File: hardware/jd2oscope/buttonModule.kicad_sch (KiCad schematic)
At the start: 1 part

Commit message: feat: lot of progress
added decoupling caps, implemented a lot more of the comm. protocol stuffs, updated BNC connector to updated version, added more notes for GPIO pin I/O for future code implementation, lot of other stuff too (frankly can't remember all of it lol); I commit here b/c want to back up progress b/4 I go get smth to eat ;)
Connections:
- net GND: now reaches S1.1
- net GPIOpin: now reaches S1.3
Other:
- note added: "How the button works w/ any given GPIO pin: (GPIO pin's initial state should be set as "HIGH" in the code) an interrupt should be set to trigger if GPIO drops below a certain V (i.e., 0V to represent GND; thus: whenever the button is pressed down, the interrupt is triggered & allows us to execute code from it"
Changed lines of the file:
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@@
 	(generator_version "8.0")
 	(paper "A4")
+	(rectangle
+		(start 119.38 75.692)
+		(end 189.865 86.487)
+		(stroke
+			(width 0)
+			(type default)
+		)
+		(fill
+			(type none)
+		)
+	)
+	(text "How the button works w/ any given GPIO pin:\n(GPIO pin's initial state should be set as \"HIGH\" in the code)\nan interrupt should be set to trigger if GPIO drops below a certain V\n(i.e., 0V to represent GND; thus: whenever the button is pressed down,\nthe interrupt is triggered & allows us to execute code from it"
+		(exclude_from_sim no)
+		(at 120.015 81.28 0)
+		(effects
+			(font
+				(size 1.27 1.27)
+			)
+			(justify left)
+		)
+	)
+	(hierarchical_label "GPIOpin"
+		(shape passive)
+		(at 144.78 97.79 180)
+		(effects
+			(font
+				(size 1.27 1.27)
+			)
+			(justify right)
+		)
+	)
+	(hierarchical_label "GND"
+		(shape passive)
+		(at 160.02 97.79 0)
+		(effects
+			(font
+				(size 1.27 1.27)
+			)
+			(justify left)
+		)
+	)
 	(symbol
 		(lib_id "bttn:KMR731NGLFS")

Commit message: feat: finished schematics
I think! Subject to change tho! for now though at least, I think they look clean asf hah~
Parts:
- renumbered S1 to S4
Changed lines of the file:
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@@
 		(dnp no)
 		(fields_autoplaced yes)
-		(property "Reference" "S1"
+		(property "Reference" "S4"
 			(at 152.4 90.17 0)
 			(effects
@@
 		)
 		(instances
-			(project ""
-				(path "/eb18a3da-9fbf-4329-a814-1afab785c817/53a41818-3f0f-42a5-bb8b-35a22bb57817"
+			(project "jd2oscope"
+				(path "/eb18a3da-9fbf-4329-a814-1afab785c817/415ed027-7cd2-4459-ae99-e85a85aec1e2/946e3097-58f0-4375-84c2-921a93494f1e"
+					(reference "S4")
+					(unit 1)
+				)
+				(path "/eb18a3da-9fbf-4329-a814-1afab785c817/415ed027-7cd2-4459-ae99-e85a85aec1e2/4f25ad0e-659b-4d0d-998d-272f66fe29fb/59e5b20f-a405-48c1-b2c2-d334523c9ae1"
 					(reference "S1")
 					(unit 1)
 				)
+				(path "/eb18a3da-9fbf-4329-a814-1afab785c817/415ed027-7cd2-4459-ae99-e85a85aec1e2/9cf642e2-7276-4116-93a5-7485645ddebf/59e5b20f-a405-48c1-b2c2-d334523c9ae1"
+					(reference "S2")
+					(unit 1)
+				)

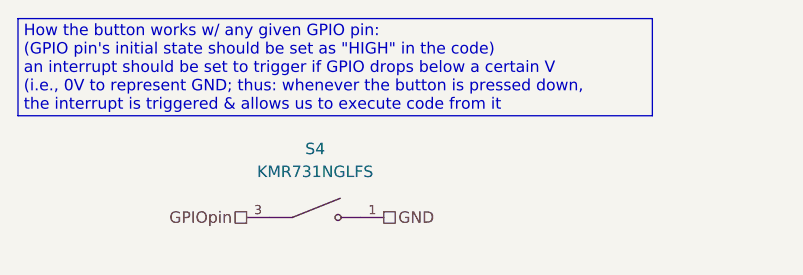
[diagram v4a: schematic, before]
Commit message: fix: ERC funtimes
fixed a bunch of dependencies with ERC checks for the schematic; shouuuuld be easier/actually possible to open on other devices now?? (added a buncha schematics & footprints to the local files & whatnot)
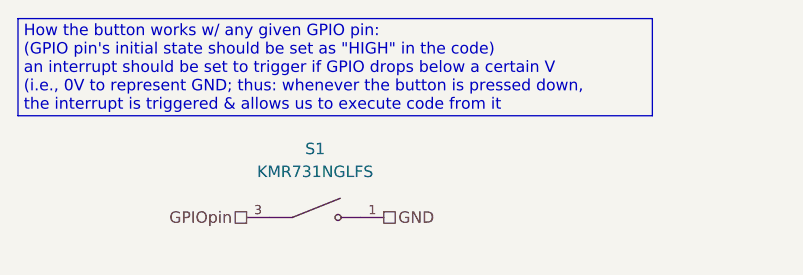
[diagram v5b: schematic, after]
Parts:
- removed S4: KMR731NGLFS, KMR731NGLFS:SW_KMR731NGLFS, symbol bttn:KMR731NGLFS
- added S1: KMR731NGLFS, KMR731NGLFS:SW_KMR731NGLFS, symbol KMR731NGLFS:KMR731NGLFS
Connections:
- net GND: now also S1.1
- net GPIOpin: now also S1.3
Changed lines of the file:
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@@
 	)
 	(symbol
-		(lib_id "bttn:KMR731NGLFS")
+		(lib_id "KMR731NGLFS:KMR731NGLFS")
 		(at 152.4 97.79 0)
 		(unit 1)
@@
 		(dnp no)
 		(fields_autoplaced yes)
-		(property "Reference" "S4"
+		(property "Reference" "S1"
 			(at 152.4 90.17 0)
 			(effects
@@
 			)
 		)
-		(property "Sim.Device" ""
-			(at 152.4 97.79 0)
-			(effects
-				(font
-					(size 1.27 1.27)
-				)
-				(hide yes)
-			)
-		)
-		(property "Sim.Params" ""
-			(at 152.4 97.79 0)
-			(effects
-				(font
-					(size 1.27 1.27)
-				)
-				(hide yes)
-			)
-		)
-		(property "Sim.Pins" ""
-			(at 152.4 97.79 0)
-			(effects
-				(font
-					(size 1.27 1.27)
-				)
-				(hide yes)
-			)
-		)
-		(property "Sim.Type" ""
-			(at 152.4 97.79 0)
-			(effects
-				(font
-					(size 1.27 1.27)
-				)
-				(hide yes)
-			)
-		)
-		(property "Comment" ""
-			(at 152.4 97.79 0)
-			(effects
-				(font
-					(size 1.27 1.27)
-				)
-				(hide yes)
-			)
-		)
-		(property "EU_RoHS_Compliance" ""
-			(at 152.4 97.79 0)
-			(effects
-				(font
-					(size 1.27 1.27)
-				)
-				(hide yes)
-			)
-		)
-		(property "Number_of_Positions" ""
-			(at 152.4 97.79 0)
-			(effects
-				(font
-					(size 1.27 1.27)
-				)
-				(hide yes)
-			)
+		(pin "1"
 		)
 		(pin "3"
-		)
-		(pin "1"
 		)
 		(instances
 			(project "jd2oscope"
 				(path "/eb18a3da-9fbf-4329-a814-1afab785c817/415ed027-7cd2-4459-ae99-e85a85aec1e2/946e3097-58f0-4375-84c2-921a93494f1e"
-					(reference "S4")
+					(reference "S2")
 					(unit 1)
 				)
@@
 				)
 				(path "/eb18a3da-9fbf-4329-a814-1afab785c817/415ed027-7cd2-4459-ae99-e85a85aec1e2/9cf642e2-7276-4116-93a5-7485645ddebf/59e5b20f-a405-48c1-b2c2-d334523c9ae1"
-					(reference "S2")
+					(reference "S3")
 					(unit 1)
 				)

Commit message: fix: footprint/symbol fixes for ILI9341_Touch
blegh
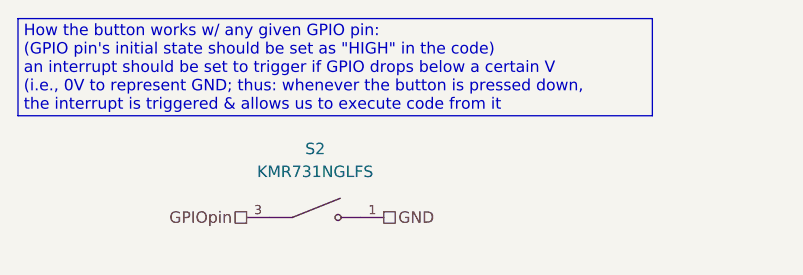
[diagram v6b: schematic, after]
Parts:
- renumbered S1 to S2
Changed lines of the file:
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@@
 		(dnp no)
 		(fields_autoplaced yes)
-		(property "Reference" "S1"
+		(property "Reference" "S2"
 			(at 152.4 90.17 0)
 			(effects

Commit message: feat/fix: no more errors for PCB import too!
Now both the ERC, and the schematic import (and my OCD) are completely satisfied, and we can dev the actual PCB; let's go!! :D
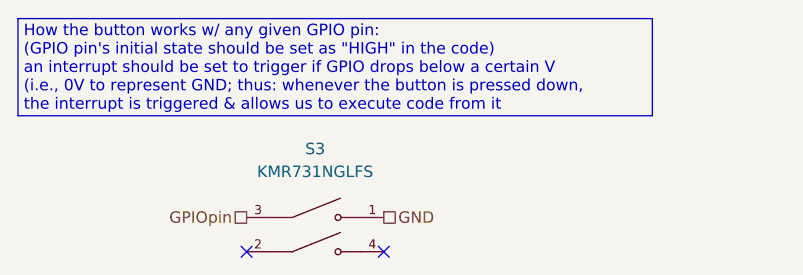
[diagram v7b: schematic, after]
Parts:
- S3: renamed from S2; footprint KMR731NGLFS:SW_KMR731NGLFS -> jd2Oscope_Footprints:SW_KMR731NGLFS
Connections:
- no-connect marks 0 -> 2
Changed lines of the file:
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@@
 	(generator_version "8.0")
 	(paper "A4")
+	(no_connect
+		(at 144.78 101.6)
+	)
+	(no_connect
+		(at 160.02 101.6)
+	)
 	(rectangle
 		(start 119.38 75.692)
@@
 		(dnp no)
 		(fields_autoplaced yes)
-		(property "Reference" "S2"
+		(property "Reference" "S3"
 			(at 152.4 90.17 0)
 			(effects
@@
 			)
 		)
-		(property "Footprint" "KMR731NGLFS:SW_KMR731NGLFS"
+		(property "Footprint" "jd2Oscope_Footprints:SW_KMR731NGLFS"
 			(at 152.4 97.79 0)
 			(effects
@@
 		)
 		(pin "3"
+		)
+		(pin "2"
+		)
+		(pin "4"
 		)
 		(instances
 			(project "jd2oscope"
 				(path "/eb18a3da-9fbf-4329-a814-1afab785c817/415ed027-7cd2-4459-ae99-e85a85aec1e2/946e3097-58f0-4375-84c2-921a93494f1e"
+					(reference "S3")
+					(unit 1)
+				)
+				(path "/eb18a3da-9fbf-4329-a814-1afab785c817/415ed027-7cd2-4459-ae99-e85a85aec1e2/4f25ad0e-659b-4d0d-998d-272f66fe29fb/59e5b20f-a405-48c1-b2c2-d334523c9ae1"
 					(reference "S2")
 					(unit 1)
 				)
-				(path "/eb18a3da-9fbf-4329-a814-1afab785c817/415ed027-7cd2-4459-ae99-e85a85aec1e2/4f25ad0e-659b-4d0d-998d-272f66fe29fb/59e5b20f-a405-48c1-b2c2-d334523c9ae1"
-					(reference "S1")
+				(path "/eb18a3da-9fbf-4329-a814-1afab785c817/415ed027-7cd2-4459-ae99-e85a85aec1e2/9cf642e2-7276-4116-93a5-7485645ddebf/59e5b20f-a405-48c1-b2c2-d334523c9ae1"
+					(reference "S4")
 					(unit 1)
 				)
-				(path "/eb18a3da-9fbf-4329-a814-1afab785c817/415ed027-7cd2-4459-ae99-e85a85aec1e2/9cf642e2-7276-4116-93a5-7485645ddebf/59e5b20f-a405-48c1-b2c2-d334523c9ae1"
-					(reference "S3")
-					(unit 1)
-				)
